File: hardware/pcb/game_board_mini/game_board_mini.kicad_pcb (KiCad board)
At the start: 2 copper layers, 248 parts, among them J1 Conn_01x08, J2 Conn_01x03_Male, J3 Conn_01x03, J4 Conn_01x03, J5 Conn_01x03, J6 USB_C_Receptacle, U1 ESP32-C3, U2 USBLC6-2SC6, Y1 Crystal_GND24

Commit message: [PCB] Routed ESP
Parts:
- removed J2: Conn_01x03_Male, Connector_PinHeader_2.54mm:PinHeader_1x03_P2.54mm_Vertical
- added JP1: SolderJumper_3_Open, Jumper:SolderJumper-3_P1.3mm_Open_Pad1.0x1.5mm, F.Cu at (142.2, 155.2)
- C73, C74, C75, C76, C77, C81, C82: footprint Capacitor_SMD:C_0805_2012Metric -> Capacitor_SMD:C_0603_1608Metric
- C78: value 1µF -> 1µ; footprint Capacitor_SMD:C_0805_2012Metric -> Capacitor_SMD:C_0603_1608Metric
- C79, C80: value 10µF -> 10µ; footprint Capacitor_SMD:C_0805_2012Metric -> Capacitor_SMD:C_0603_1608Metric
- C83, C84: value 0.1µF -> 100n; footprint Capacitor_SMD:C_0805_2012Metric -> Capacitor_SMD:C_0603_1608Metric
- J1, J6: moved to B.Cu
- L1, L2: footprint Inductor_SMD:L_0805_2012Metric -> Inductor_SMD:L_0603_1608Metric
- R77, R78, R79, R80: footprint Resistor_SMD:R_0805_2012Metric -> Resistor_SMD:R_0603_1608Metric
- moved R79 153.0 mm to (174.9, 90.0)
- moved R80 153.0 mm to (171.3, 87.4)
- moved U2 143.7 mm to (176.4, 85.7)
- moved J6 118.2 mm to (158.7, 84.8)
- moved AE1 98.3 mm to (161.5, 123.4), turned to 90 degrees
- moved C78 96.1 mm to (173.4, 124.6), turned to 180 degrees
- moved C80 93.6 mm to (164.8, 129.4)
- moved C79 93.4 mm to (170.9, 122.1), turned to 90 degrees
- moved C81 92.9 mm to (166.4, 129.4)
- moved C75 92.6 mm to (166.4, 126.4)
- moved C84 92.3 mm to (175.1, 134.6), turned to -90 degrees
- moved L2 92.1 mm to (168.7, 128.7)
- moved C73 92.0 mm to (174.2, 119.8)
- moved L1 91.9 mm to (168.7, 127.1)
- moved C82 91.5 mm to (170.9, 129.4)
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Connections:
- AE1 pad 1: GND -> /ESP-C3/ANT_PAD1
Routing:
- net /Din_BASE: track 0.00 -> 24.6 mm, vias 0 -> 2
- net GND: track 0.00 -> 16.9 mm, vias 0 -> 5
- net +3.3V: track 4.27 -> 15.6 mm
- net Net-(AE1-Pad2): track 2.01 -> 8.11 mm
- net Net-(J6-PadA7): track 4.84 -> 0.00 mm
- net Net-(C8-Pad1): track 3.30 -> 6.85 mm
- net Net-(J6-PadA6): track 3.23 -> 0.00 mm
- net Net-(C7-Pad1): track 3.30 -> 6.34 mm
- net VBUS: track 2.81 -> 0.00 mm
- net +3.3VA: track 8.72 -> 5.92 mm
- net Net-(D42-Pad2): track 9.85 -> 12.2 mm
- net Net-(D41-Pad2): track 9.84 -> 12.0 mm
- net Net-(C43-Pad1): track 3.30 -> 5.37 mm
- net /ESP-C3/LNA_IN: track 5.50 -> 4.03 mm
- net Net-(C74-Pad1): track 11.8 -> 10.7 mm
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- added copper zone on F.Cu, net /ESP-C3/ANT_PAD1
- added copper zone on B.Cu, net GND
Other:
- board outline added: 81.3 x 83.8 mm

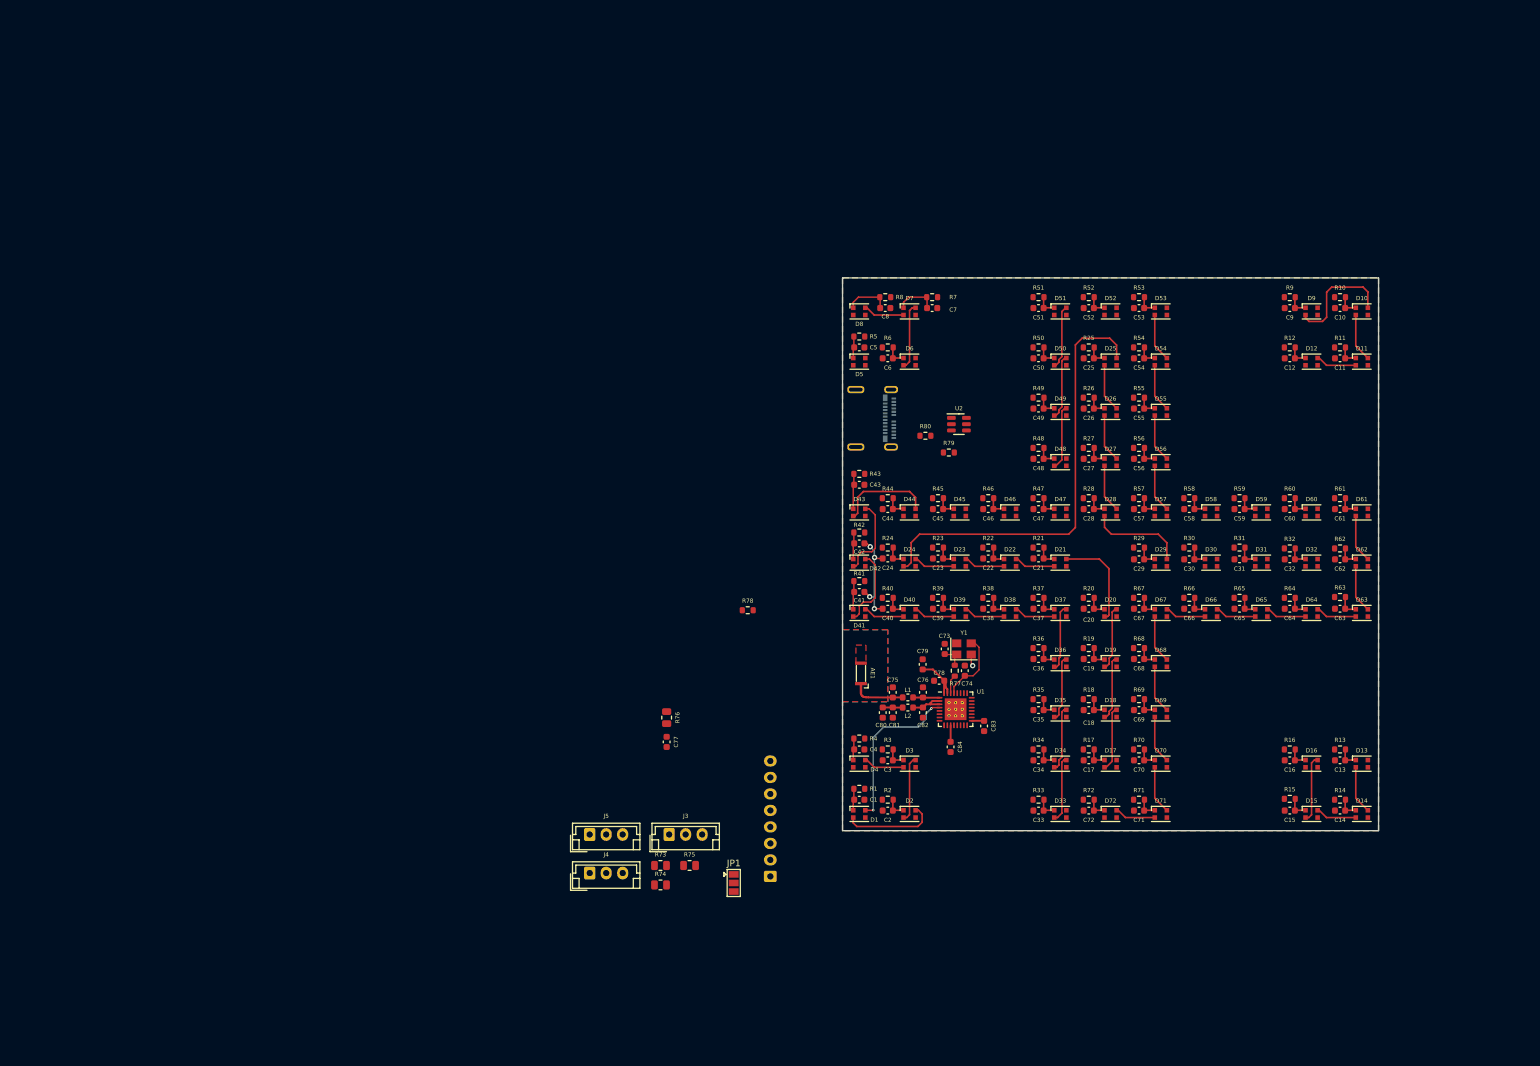
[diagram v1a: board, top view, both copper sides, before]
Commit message: [PCB] Increased board size
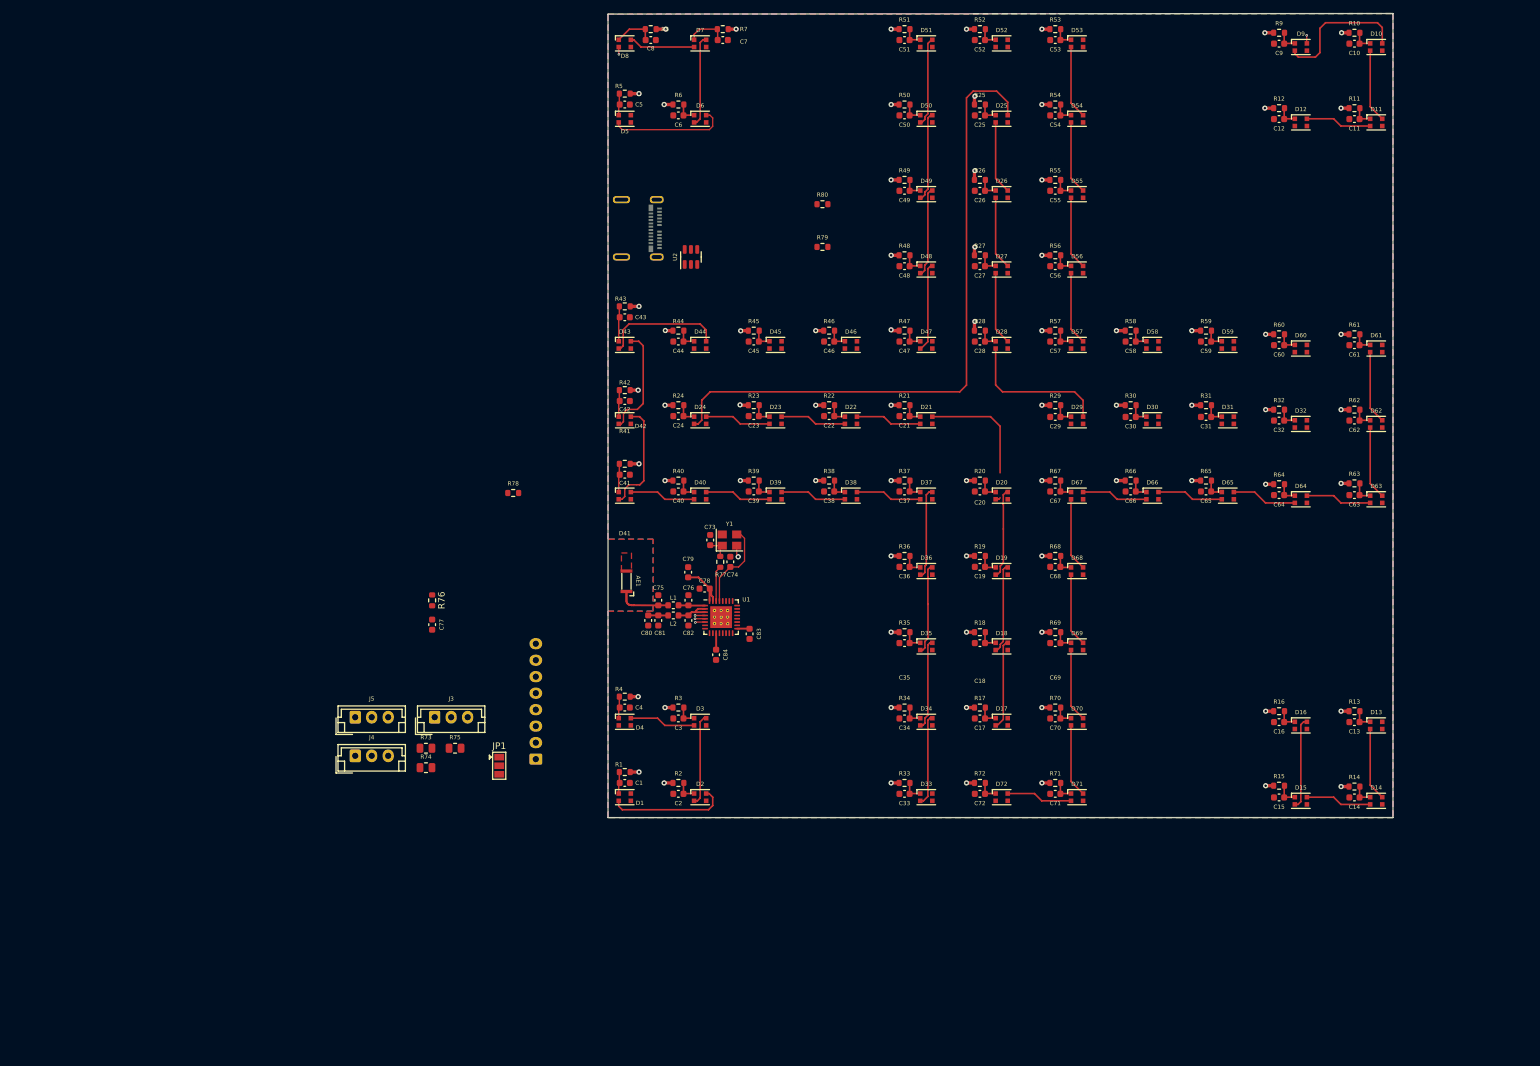
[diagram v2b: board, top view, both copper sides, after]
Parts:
- R76: footprint Resistor_SMD:R_0805_2012Metric -> Resistor_SMD:R_0603_1608Metric
- moved C8 54.0 mm to (129.7, 27.4)
- moved R8 54.0 mm to (129.7, 25.8)
- moved D8 54.0 mm to (125.7, 27.9)
- moved R7 51.6 mm to (140.6, 25.8)
- moved C7 51.6 mm to (140.6, 27.4)
- moved D7 51.6 mm to (137.2, 27.9)
- moved D5 51.2 mm to (125.7, 39.4)
- moved C5 51.2 mm to (125.7, 37.2)
- moved R5 51.2 mm to (125.7, 35.6)
- moved D6 48.6 mm to (137.2, 39.4)
- moved C6 48.6 mm to (133.9, 38.9)
- moved R6 48.6 mm to (133.9, 37.2)
- moved U2 47.9 mm to (135.8, 60.3), turned to 90 degrees
- moved J6 45.7 mm to (123.2, 56.0)
- moved D51 45.4 mm to (171.4, 27.9)
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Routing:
- net +5V: track 0.11 -> 89.4 mm, vias 0 -> 72
- net Net-(D24-Pad2): track 67.0 -> 98.4 mm
- net /Din_BASE: track 24.6 -> 1.51 mm, vias 2 -> 1
- net Net-(D5-Pad2): track 0.00 -> 17.7 mm
- net GND: track 16.9 -> 1.78 mm, vias 5 -> 1
- net Net-(D47-Pad2): track 0.00 -> 13.5 mm
- net Net-(D28-Pad2): track 14.6 -> 22.2 mm
- net Net-(D41-Pad2): track 12.0 -> 17.0 mm
- net Net-(D42-Pad2): track 12.2 -> 16.7 mm
- net Net-(D35-Pad2): track 9.92 -> 14.1 mm
- net Net-(D3-Pad2): track 6.25 -> 10.1 mm
- net Net-(D13-Pad2): track 7.28 -> 11.1 mm
- net Net-(D40-Pad2): track 6.25 -> 10.1 mm
- net Net-(D34-Pad2): track 9.91 -> 13.7 mm
- net Net-(D7-Pad2): track 6.25 -> 10.1 mm
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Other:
- board size 81.3 x 83.8 mm -> 119 x 121.9 mm

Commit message: Fixed bug: `player_count` and `brightness` reset in loop
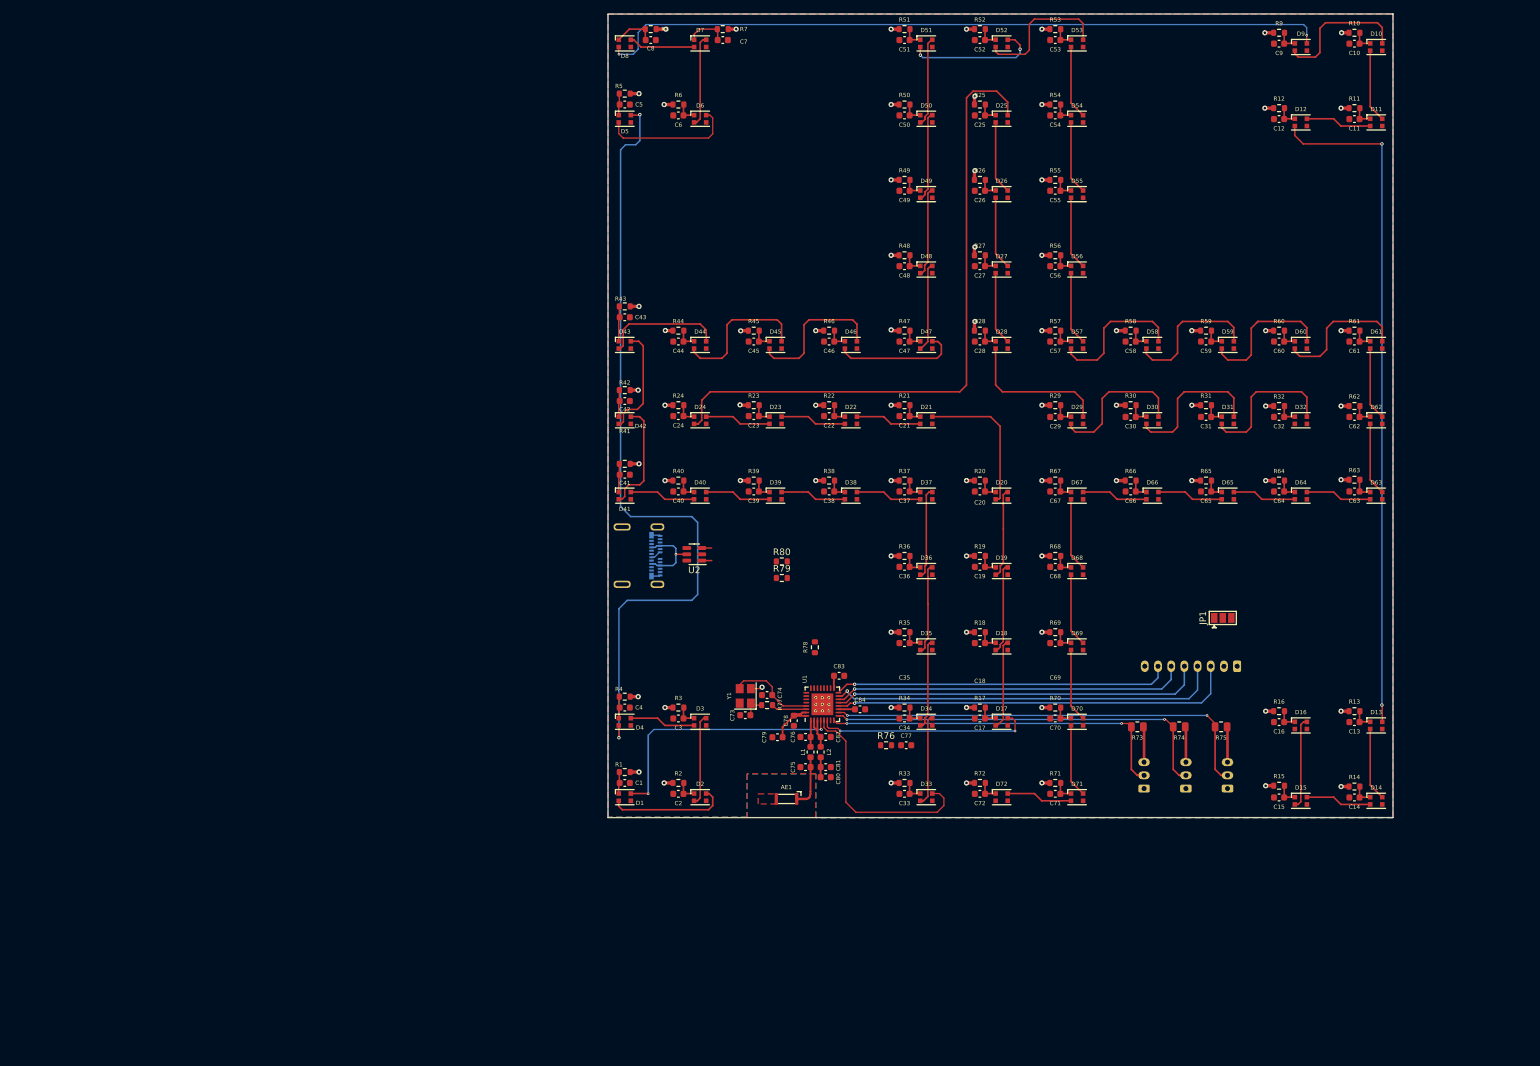
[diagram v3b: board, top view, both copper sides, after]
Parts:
- removed J6: USB_C_Receptacle, USB_C:USB_C_MOLEX_1054500101
- added J2: USB_C_Receptacle, USB_C:USB_C_MOLEX_1054500101, B.Cu at (123.3, 105.6)
- J1: footprint Connector_JST:JST_EH_B8B-EH-A_1x08_P2.50mm_Vertical -> Connector_JST:JST_PH_B8B-PH-K_1x08_P2.00mm_Vertical
- J3, J4, J5: footprint Connector_JST:JST_EH_B3B-EH-A_1x03_P2.50mm_Vertical -> Connector_JST:JST_PH_B3B-PH-K_1x03_P2.00mm_Vertical; moved to B.Cu
- moved J5 132.7 mm to (217.1, 140.9), turned to 90 degrees
- moved J4 126.1 mm to (210.8, 140.9), turned to 90 degrees
- moved R75 116.2 mm to (216.2, 131.6), turned to 180 degrees
- moved R74 114.4 mm to (209.8, 131.6), turned to 180 degrees
- moved JP1 112.0 mm to (216.4, 115.1), turned to 0 degrees
- moved J3 108.1 mm to (204.5, 140.9), turned to 90 degrees
- moved R73 107.9 mm to (203.5, 131.6), turned to 180 degrees
- moved J1 107.3 mm to (218.6, 122.4), turned to 180 degrees
- moved C77 74.2 mm to (168.4, 134.4), turned to 0 degrees
- moved R76 72.3 mm to (165.4, 134.4), turned to 0 degrees
- moved R80 54.5 mm to (149.5, 106.5)
- moved R78 51.4 mm to (154.6, 119.5), turned to 90 degrees
- moved R79 50.6 mm to (149.5, 109.0)
- moved U2 45.1 mm to (136.3, 105.4), turned to 180 degrees
- moved AE1 41.0 mm to (150.2, 142.5), turned to 180 degrees
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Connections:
- C78 pad 1: +3.3V -> +3V3
- C79 pad 1: +3.3V -> +3V3
- C80 pad 1: +3.3V -> +3V3
- C81 pad 1: +3.3V -> +3V3
- C83 pad 1: +3.3V -> +3V3
- C84 pad 1: +3.3V -> +3V3
- L2 pad 1: +3.3V -> +3V3
- R73 pad 1: +5V -> +3V3
- R74 pad 1: +5V -> +3V3
- R75 pad 1: +5V -> +3V3
- R76 pad 1: +3.3V -> +3V3
- R79 pad 1: /ESP-C3/CC1 -> /USB_C/CC1
- R80 pad 1: /ESP-C3/CC2 -> /USB_C/CC2
- U1 pad 11: +3.3V -> +3V3
- U1 pad 17: +3.3V -> +3V3
- U1 pad 31: +3.3V -> +3V3
- U1 pad 32: +3.3V -> +3V3
- U2 pad 4: Net-(J6-PadA6) -> /USB_C/USB_NO_ESD_D+
- U2 pad 6: Net-(J6-PadA7) -> /USB_C/USB_NO_ESD_D-
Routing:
- net Net-(D4-Pad2): track 0.00 -> 120.8 mm, vias 0 -> 2
- net Net-(D8-Pad2): track 2.35 -> 111.3 mm
- net Net-(D12-Pad2): track 0.00 -> 102.8 mm, vias 0 -> 2
- net /Button_3: track 0.00 -> 67.0 mm, vias 0 -> 2
- net /CS: track 0.00 -> 61.4 mm, vias 0 -> 1
- net /Button_2: track 0.00 -> 60.2 mm, vias 0 -> 2
- net /SCK: track 0.00 -> 59.5 mm, vias 0 -> 1
- net /DC: track 0.00 -> 56.4 mm, vias 0 -> 1
- net /Button_1: track 0.00 -> 54.3 mm, vias 0 -> 2
- net /RST: track 0.00 -> 53.7 mm, vias 0 -> 1
- net /MOSI: track 0.00 -> 51.1 mm, vias 0 -> 1
- net /Din_BASE: track 1.51 -> 39.7 mm, vias 1 -> 2
- net /Din_FIELD: track 1.76 -> 33.6 mm, vias 1 -> 0
- net +3V3: track 0.00 -> 31.7 mm
- net /Din_GOAL: track 1.50 -> 32.5 mm, vias 1 -> 2
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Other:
- outline, holes or cut-outs redrawn
- board text added: "+5V"
- board text added: "BL/ LED"
- board text added: "CS"
- board text added: "DC"
- board text added: "GND"
- board text added: "RST"
- board text added: "SCK"
- board text added: "SDA/ MOSI"

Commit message: [PCB] Current board
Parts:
- moved J5 1.19 mm to (218.3, 140.9)
- moved JP1 1.15 mm to (215.3, 114.9)
- moved R75 1.10 mm to (217.3, 131.6)
- moved J4 0.55 mm to (211.4, 140.9)
- moved R74 0.51 mm to (210.3, 131.6)
- moved J3 0.09 mm to (204.4, 140.9)
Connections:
- net /ESP-C3/GPIO_21 renamed /Connectors/EN_TFT
- net /LED / BL renamed /Connectors/LED / BL
- J1 pad 8: +5V -> unconnected-(J1-Pad8)
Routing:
- net /Button_3: track 67.0 -> 68.3 mm
- net /Button_2: track 60.2 -> 60.7 mm
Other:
- board text added: "3V3"
- board text added: "IN"
